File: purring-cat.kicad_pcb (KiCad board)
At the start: 2 copper layers, 53.4 x 93.5 mm, 8 parts, among them M1 Motor_DC, SW1 SW_Push

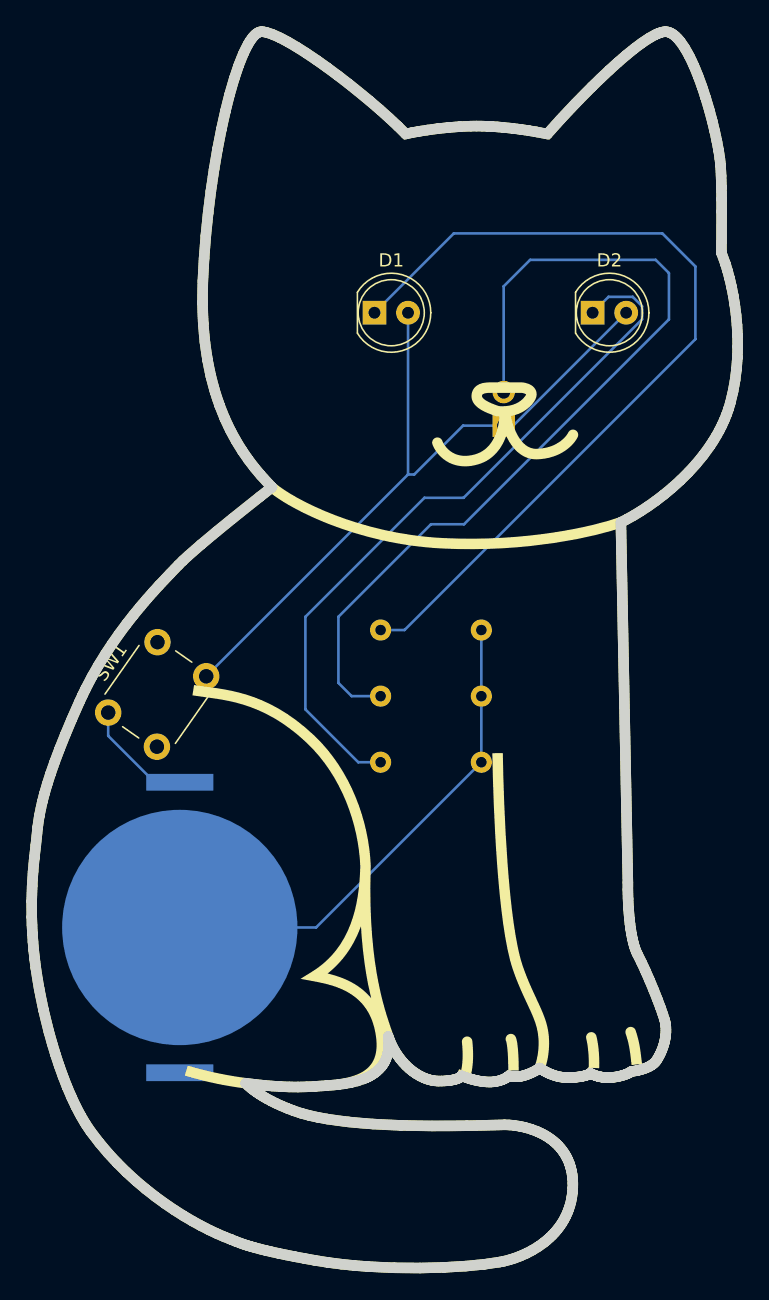
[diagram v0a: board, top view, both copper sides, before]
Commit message: Add backside of cat
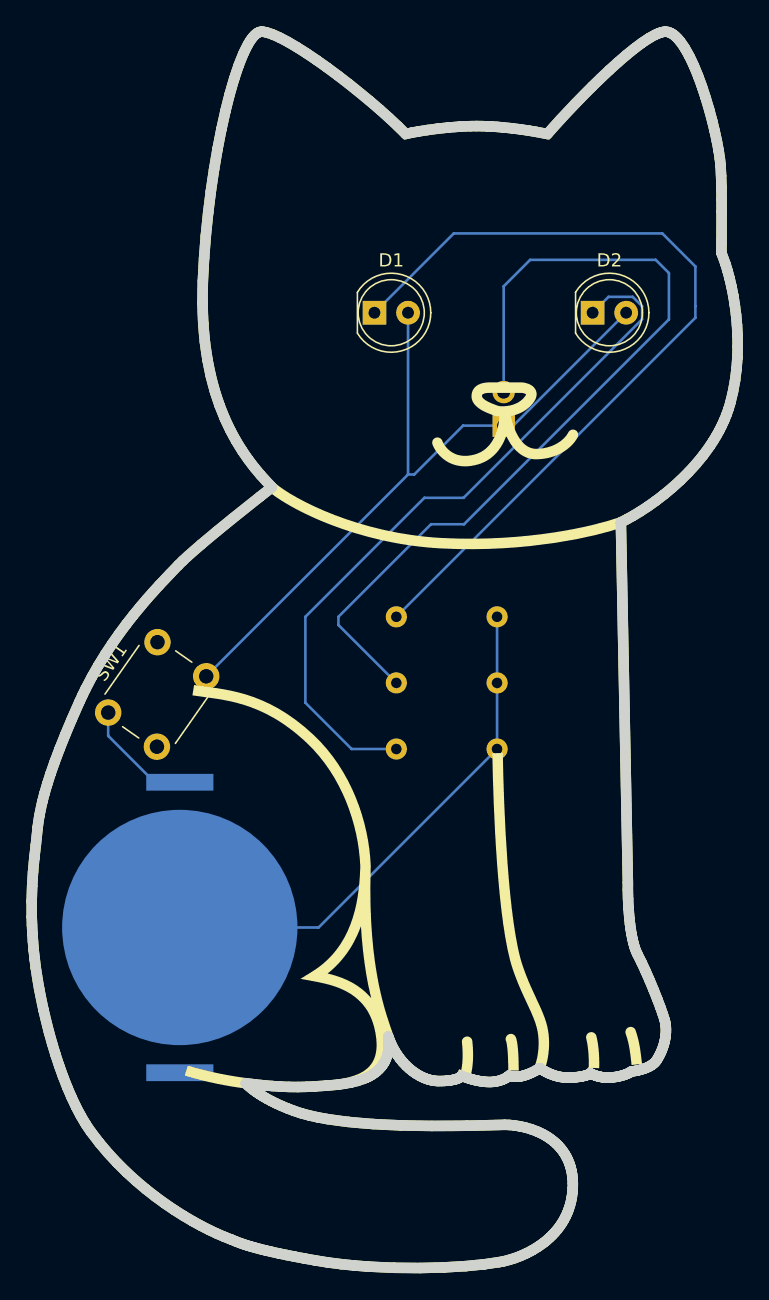
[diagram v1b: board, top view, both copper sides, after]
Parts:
- moved R1 1.55 mm to (205.5, 93.5)
- moved R2 1.55 mm to (197.9, 103.5)
- moved R3 1.55 mm to (197.9, 98.5)
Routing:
- net Net-(D1-K): track 66.2 -> 63.7 mm
- net Net-(M1--): track 68.2 -> 66.4 mm
- net Net-(BT1--): track 38.0 -> 39.6 mm
